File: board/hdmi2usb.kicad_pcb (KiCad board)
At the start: 8 copper layers, 177.8 x 106.7 mm, 313 parts, among them J1 USB_MICRO_B, J2 HDMI, J3 HDMI, J4 HDMI, J5 DVI-STACKED, J6 DVI-STACKED, J7 HDMI, J8 VHDCI, J9 DVI-STACKED, P1 CONN_7X2, U1 CY7C68013A, U10 IP4776CZ38, U11 IP4776CZ38, U12 SPARTAN6LXXXX-CSG324, U13 FXO-HC536R, U2 M25P16, U3 LMR10530, U4 LMR10530, U5 LMR10530, U6 LP2997, U7 MT47H64M16HR, U8 IP4776CZ38, U9 IP4776CZ38, X1 CRYSTAL

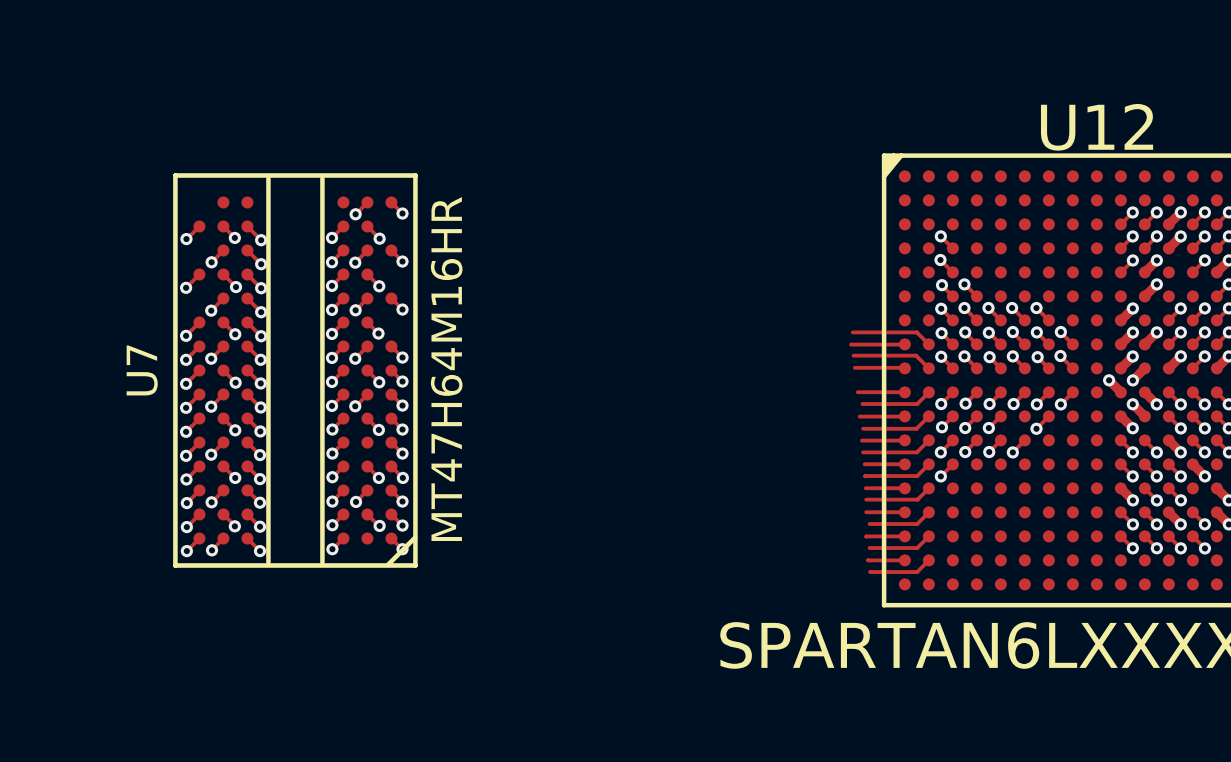
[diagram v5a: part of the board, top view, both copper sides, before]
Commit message: Issue #510 - DDR routing just completed
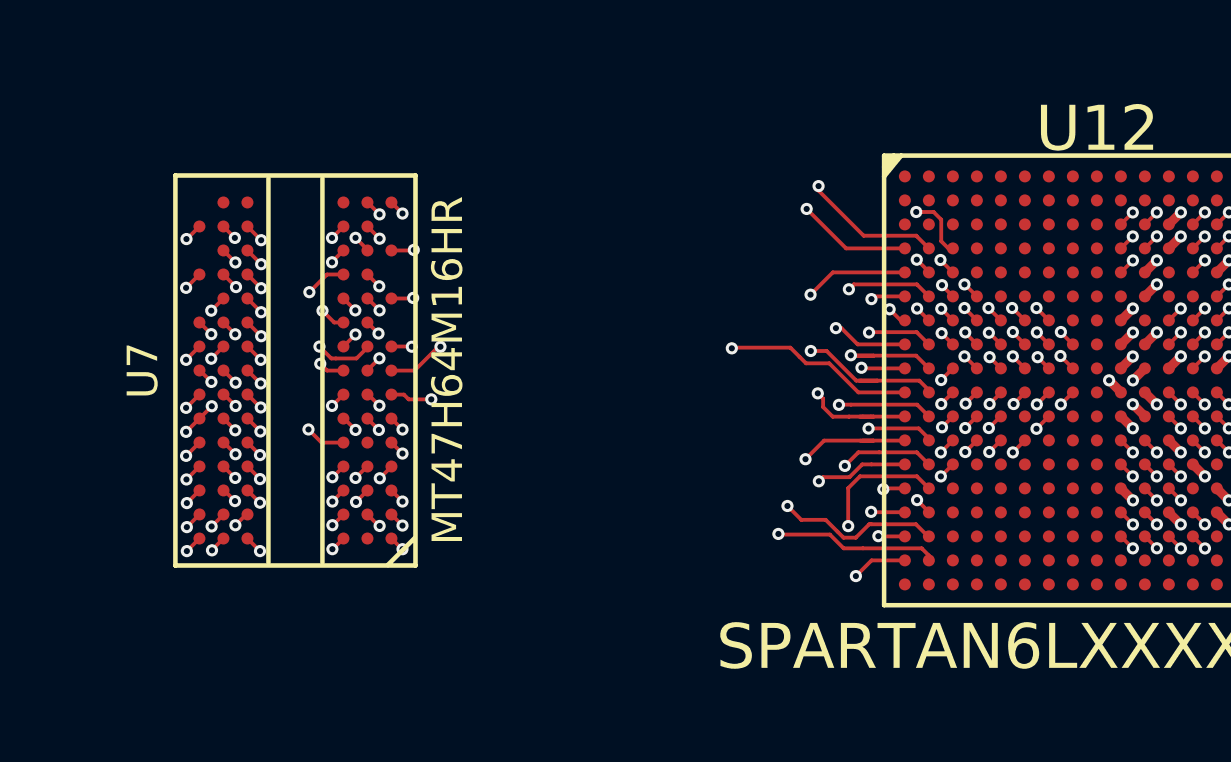
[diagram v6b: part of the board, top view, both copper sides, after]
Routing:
- net /MT47H64M16HR/DDR-LDQS_P: track 1.16 -> 36.9 mm
- net /MT47H64M16HR/DDR-D7: track 2.31 -> 37.1 mm, vias 1 -> 3
- net /MT47H64M16HR/DDR-D2: track 3.00 -> 37.7 mm, vias 1 -> 2
- net /MT47H64M16HR/DDR-D11: track 1.86 -> 35.7 mm, vias 1 -> 2
- net /MT47H64M16HR/DDR-D6: track 1.08 -> 34.4 mm
- net /MT47H64M16HR/DDR-D3: track 2.11 -> 35.0 mm, vias 1 -> 2
- net /MT47H64M16HR/DDR-A3: track 1.17 -> 32.9 mm
- net /MT47H64M16HR/DDR-D9: track 1.97 -> 33.5 mm, vias 1 -> 2
- net /MT47H64M16HR/DDR-A2: track 1.21 -> 32.6 mm
- net /MT47H64M16HR/DDR-ODT: track 1.17 -> 32.5 mm
- net /MT47H64M16HR/DDR-A0: track 1.15 -> 31.8 mm
- net /MT47H64M16HR/DDR-D13: track 1.91 -> 31.7 mm, vias 1 -> 2
- net /MT47H64M16HR/DDR-D5: track 2.43 -> 32.2 mm, vias 1 -> 2
- net /MT47H64M16HR/DDR-LDQS_N: track 1.09 -> 30.6 mm
- net /MT47H64M16HR/DDR-D14: track 2.64 -> 31.5 mm, vias 1 -> 2
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
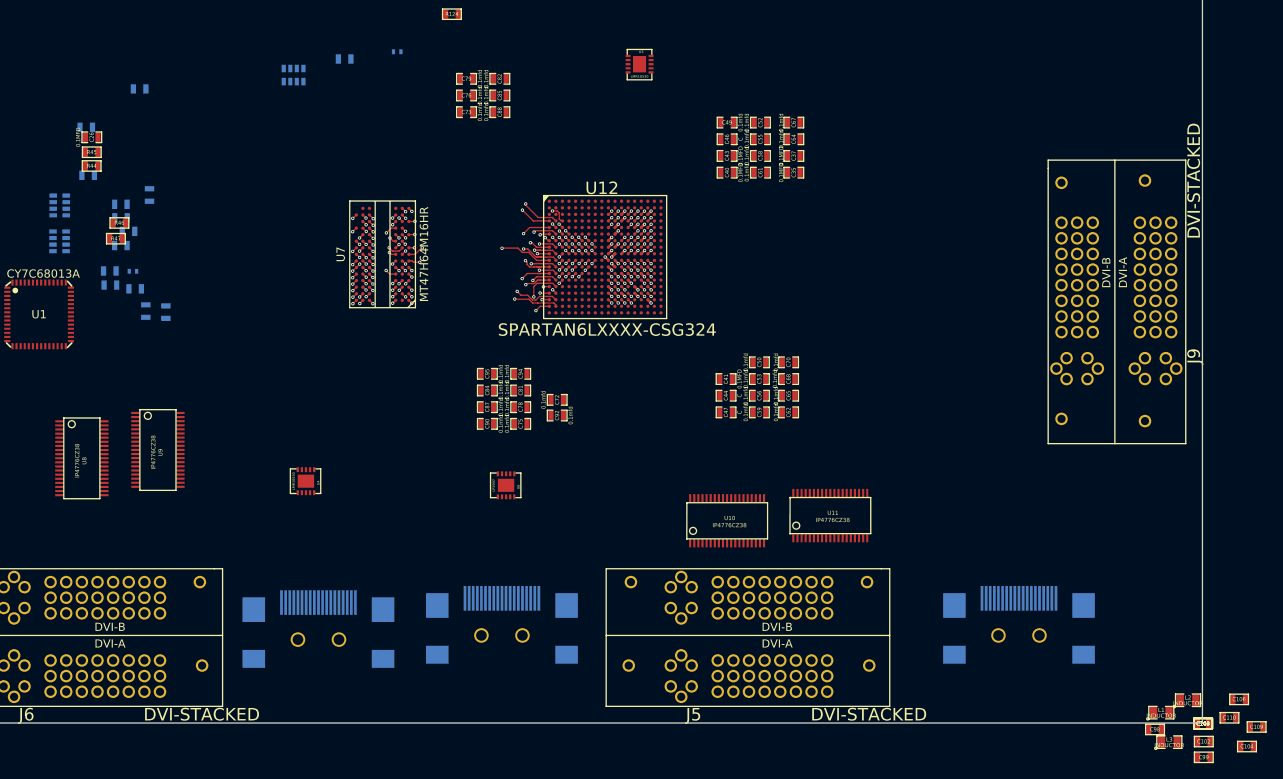
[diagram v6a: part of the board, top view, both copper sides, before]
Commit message: Issue #510 - Length Matching Started.
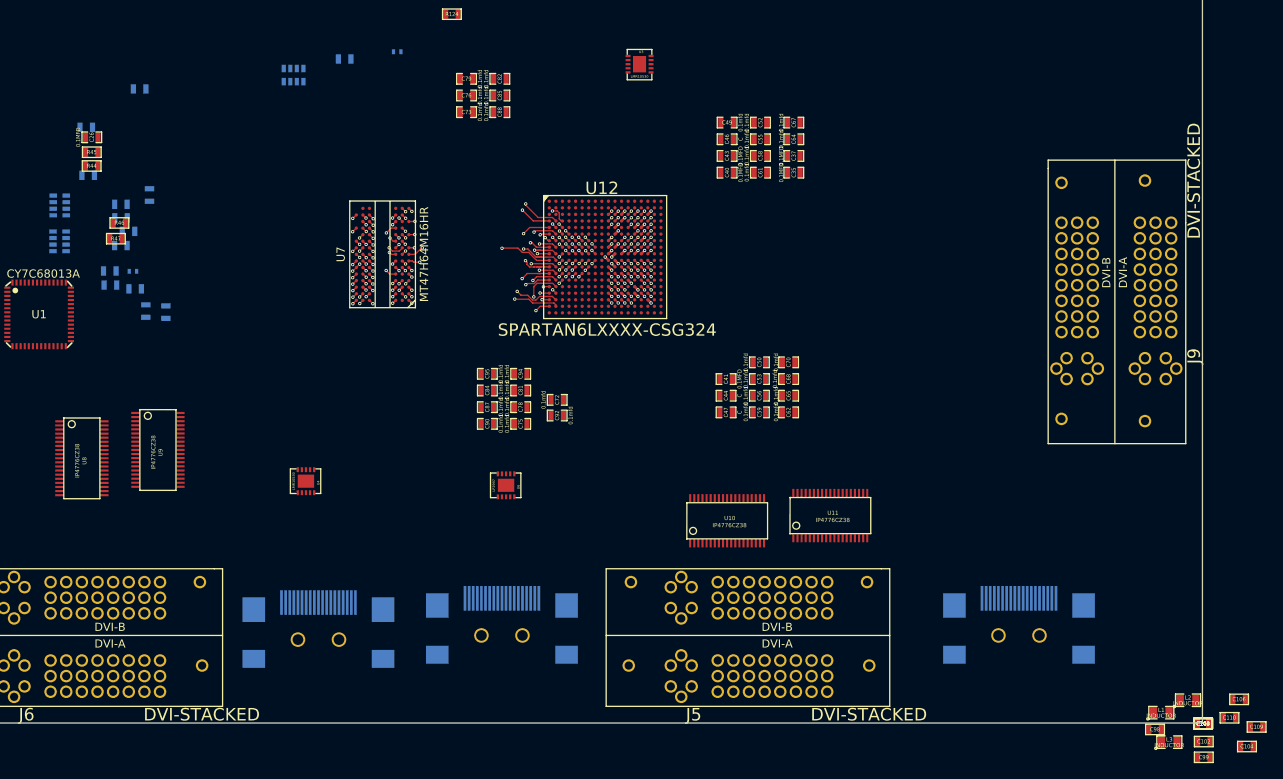
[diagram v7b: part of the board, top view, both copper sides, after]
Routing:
- net /MT47H64M16HR/DDR-WE: track 23.2 -> 31.6 mm
- net /MT47H64M16HR/DDR-CK_N: track 25.4 -> 31.8 mm
- net /MT47H64M16HR/DDR-CK_P: track 28.6 -> 31.7 mm

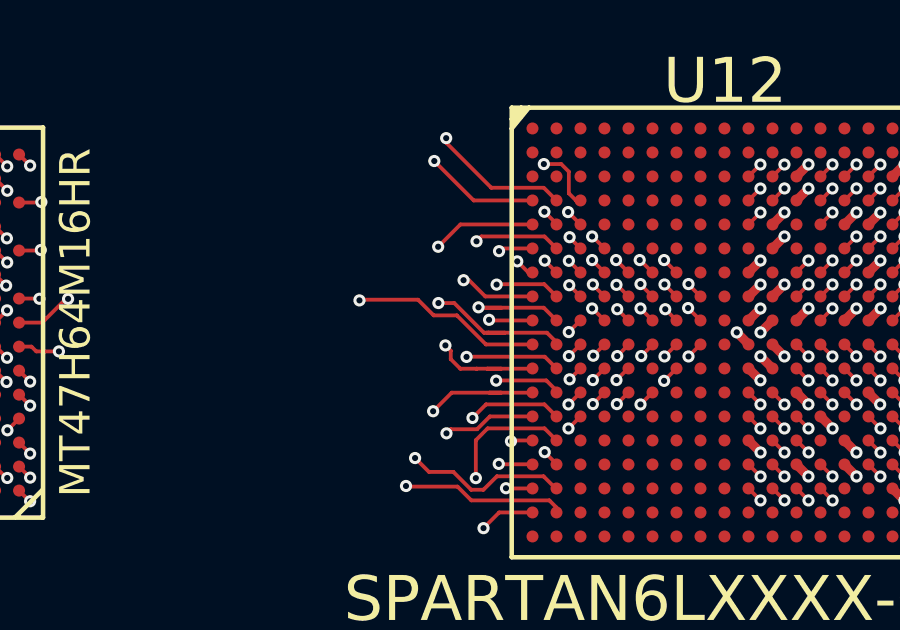
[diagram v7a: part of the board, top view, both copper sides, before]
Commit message: Issue #510 - Length Matching completed in the following sections D0-D15, CKE,CK_P,CK_N,LDM,UDM,LDQS_N,UDQS_N,LDQS_P,UDQS_P,WE. length matched between 31.6 to 31.8 mm.
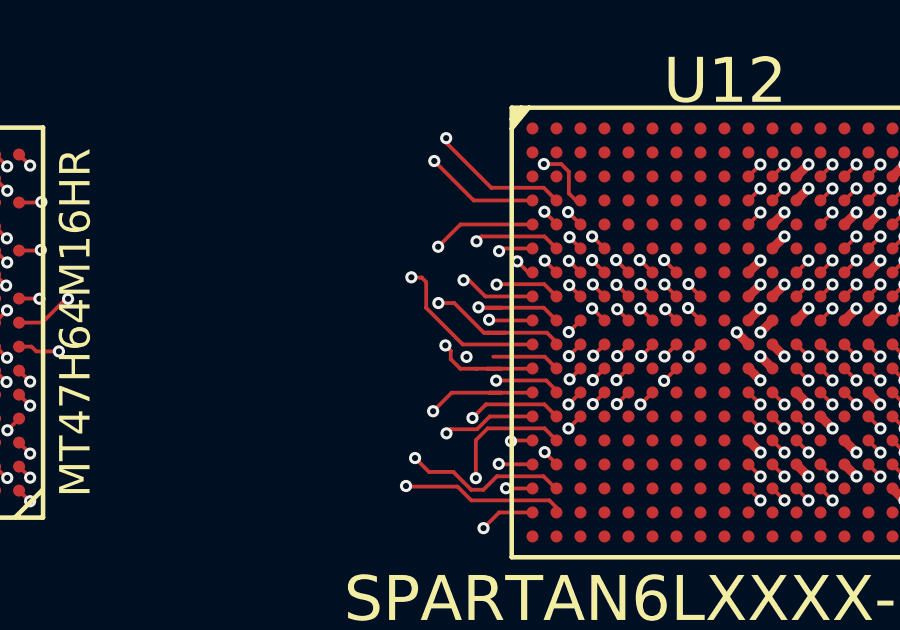
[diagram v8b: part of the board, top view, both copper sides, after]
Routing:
- net /MT47H64M16HR/DDR-CKE: track 23.8 -> 31.8 mm
- net /MT47H64M16HR/DDR-D2: track 37.7 -> 31.6 mm
- net /MT47H64M16HR/DDR-D0: track 26.2 -> 31.6 mm
- net /MT47H64M16HR/DDR-D7: track 37.1 -> 31.6 mm
- net /MT47H64M16HR/DDR-LDQS_P: track 36.9 -> 31.7 mm
- net /MT47H64M16HR/DDR-D1: track 26.5 -> 31.7 mm
- net /MT47H64M16HR/DDR-D11: track 35.6 -> 31.8 mm
- net /MT47H64M16HR/DDR-UDQS_N: track 27.8 -> 31.6 mm
- net /MT47H64M16HR/DDR-D15: track 28.0 -> 31.8 mm
- net /MT47H64M16HR/DDR-D12: track 28.2 -> 31.7 mm
- net /MT47H64M16HR/DDR-D3: track 35.0 -> 31.8 mm
- net /MT47H64M16HR/DDR-D8: track 28.8 -> 31.7 mm
- net /MT47H64M16HR/DDR-UDM: track 28.9 -> 31.8 mm
- net /MT47H64M16HR/DDR-D6: track 34.4 -> 31.6 mm
- net /MT47H64M16HR/DDR-UDQS_P: track 29.1 -> 31.7 mm
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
